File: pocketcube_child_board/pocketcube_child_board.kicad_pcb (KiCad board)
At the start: 2 copper layers, 50 x 50 mm, 3 parts, among them J1 M55-7101242R

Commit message: Fixed footprints
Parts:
- moved MOD1 0.54 mm to (106.0, 68.5)
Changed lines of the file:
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@@
 	(footprint "inspirefly:RFM98W-433S2"
 		(layer "F.Cu")
-		(at 106.2 68)
+		(at 106 68.5)
 		(property "Reference" "MOD1"
 			(at -4.825 -9.075 0)
@@
 		)
 		(embedded_fonts no)
-		(model "/Users/alexdiarra/Desktop/RFM98W-433S2.STEP 14.24.08"
+		(model "${KIPRJMOD}/3D Files/RFM98W-433S2.STEP"
 			(offset
 				(xyz 0 0 0)
@@
 		)
 		(embedded_fonts no)
-		(model "/Users/alexdiarra/Downloads/RF_Copper_Antenna_Model.STEP"
+		(model "${KIPRJMOD}/3D Files/RF_Copper_Antenna_Model.STEP"
 			(offset
 				(xyz 0 84.5 2)
@@
 		)
 		(embedded_fonts no)
-		(model "/Users/alexdiarra/Desktop/m55-7101242r.stp"
+		(model "${KIPRJMOD}/3D Files/m55-7101242r.stp"
 			(offset
 				(xyz 0 2.59 2)
@@
 		)
 	)
+	(gr_line
+		(start 115.5 75.5)
+		(end 126.5 75.5)
+		(stroke
+			(width 0.2)
+			(type default)
+		)
+		(layer "F.Cu")
+	)
+	(gr_line
+		(start 127.5 74.5)
+		(end 127.5 60.5)
+		(stroke
+			(width 0.2)
+			(type default)
+		)
+		(layer "F.Cu")
+	)
+	(gr_line
+		(start 126.5 75.5)
+		(end 127.5 74.5)
+		(stroke
+			(width 0.2)
+			(type default)
+		)
+		(layer "F.Cu")
+	)
 	(gr_rect

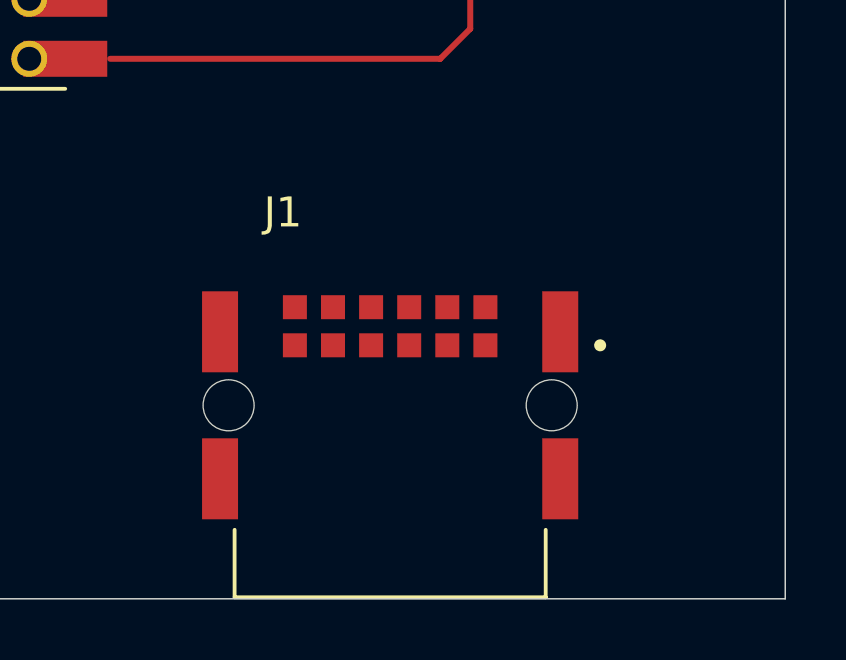
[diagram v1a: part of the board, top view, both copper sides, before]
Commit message: Added new connector to PCB
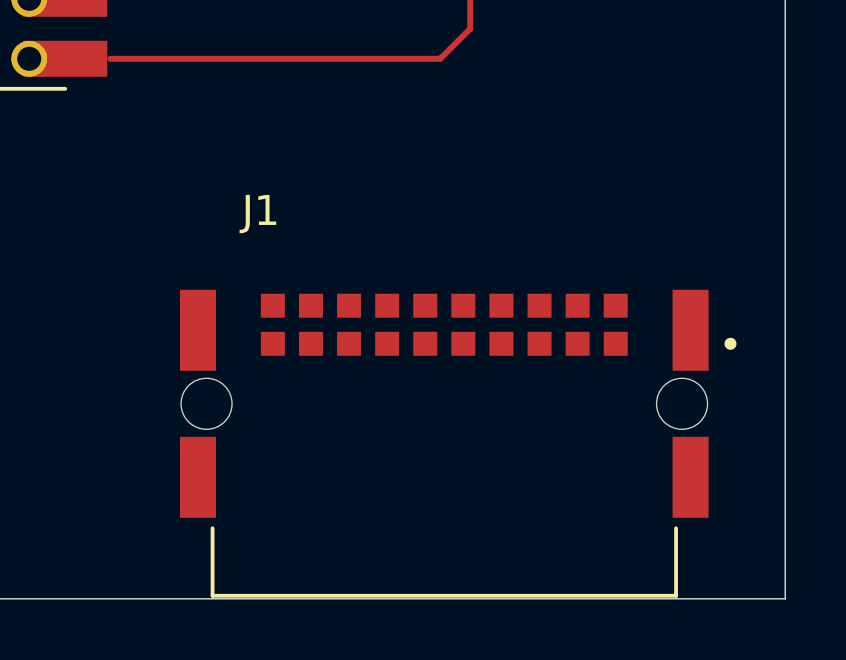
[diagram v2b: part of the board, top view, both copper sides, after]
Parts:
- J1: value M55-7101242R -> M55-7102042R; footprint inspirefly:HARWIN_M55-7101242R -> inspirefly:HARWIN_M55-7102042R
- moved J1 1.81 mm to (126.6, 87.0)
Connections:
- J1 pad A1: 3.3V -> unconnected-(J1-PadA1)
- J1 pad A2: CLK -> unconnected-(J1-PadA2)
- J1 pad A3: CS -> unconnected-(J1-PadA3)
- J1 pad A4: MISO -> 4.2V
- J1 pad A5: MOSI -> 3.3V
- J1 pad A6: GND -> CLK
- J1 pad B1: 3.3V -> unconnected-(J1-PadB1)
- J1 pad B2: CLK -> unconnected-(J1-PadB2)
- J1 pad B3: CS -> unconnected-(J1-PadB3)
- J1 pad B4: MISO -> 4.2V
- J1 pad B5: MOSI -> 3.3V
- J1 pad B6: GND -> CLK

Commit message: 11/2 via stitching v0.1
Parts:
- moved J1 27.9 mm to (104.5, 70.0)
- moved MOD1 16.1 mm to (104.0, 52.5)
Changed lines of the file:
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@@
 			(psa4output no)
 			(plot_black_and_white yes)
-			(plotinvisibletext no)
 			(sketchpadsonfab no)
 			(plotpadnumbers no)
@@
 	(footprint "inspirefly:RFM98W-433S2"
 		(layer "F.Cu")
-		(at 106 68.5)
+		(at 104 52.5)
 		(property "Reference" "MOD1"
 			(at -4.825 -9.075 0)
@@
 	(footprint "inspirefly:HARWIN_M55-7102042R"
 		(layer "F.Cu")
-		(at 126.635 87)
+		(at 104.5 70)
 		(property "Reference" "J1"
 			(at -6.115 -6.425 0)

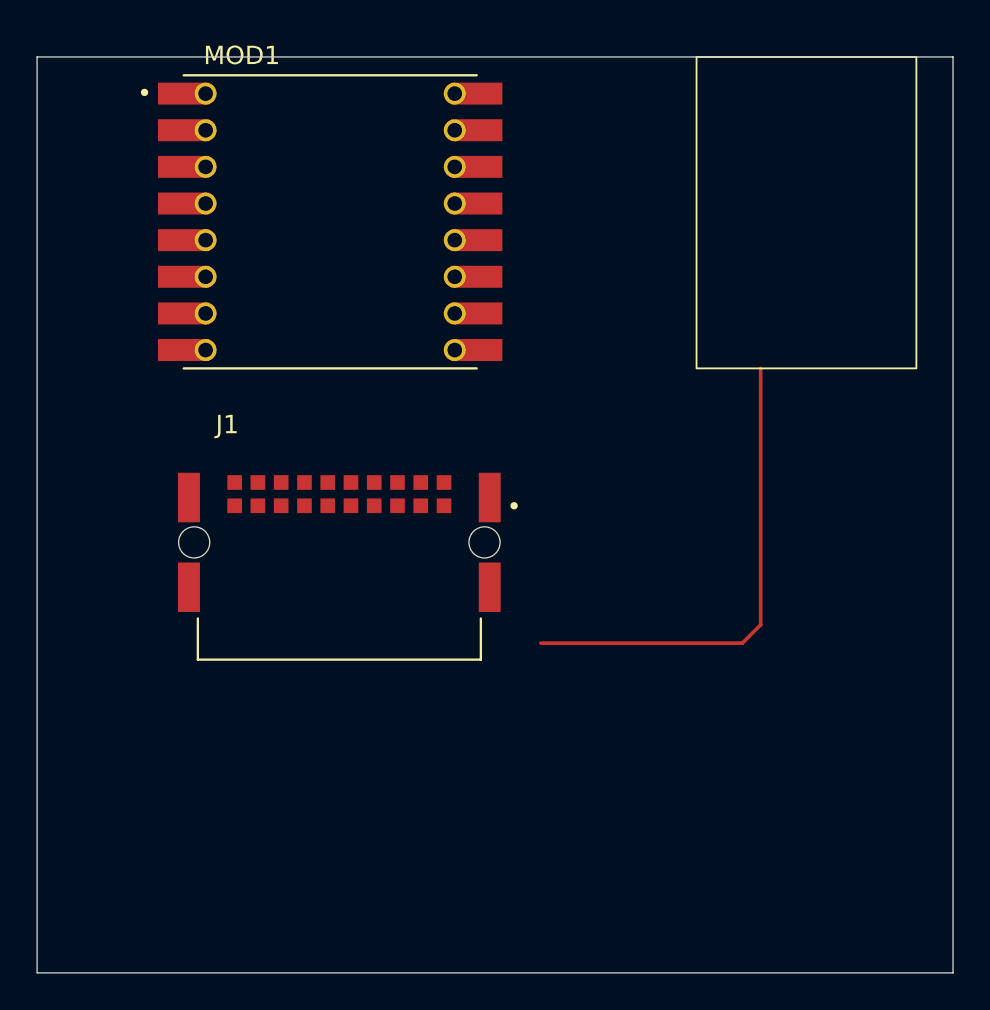
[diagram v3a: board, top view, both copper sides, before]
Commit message: Edited PCB Layout & Rearranged Pins
I restructured the layout of the PCB due to traces going under the components, I also changed the pin order of the connector to add with routing
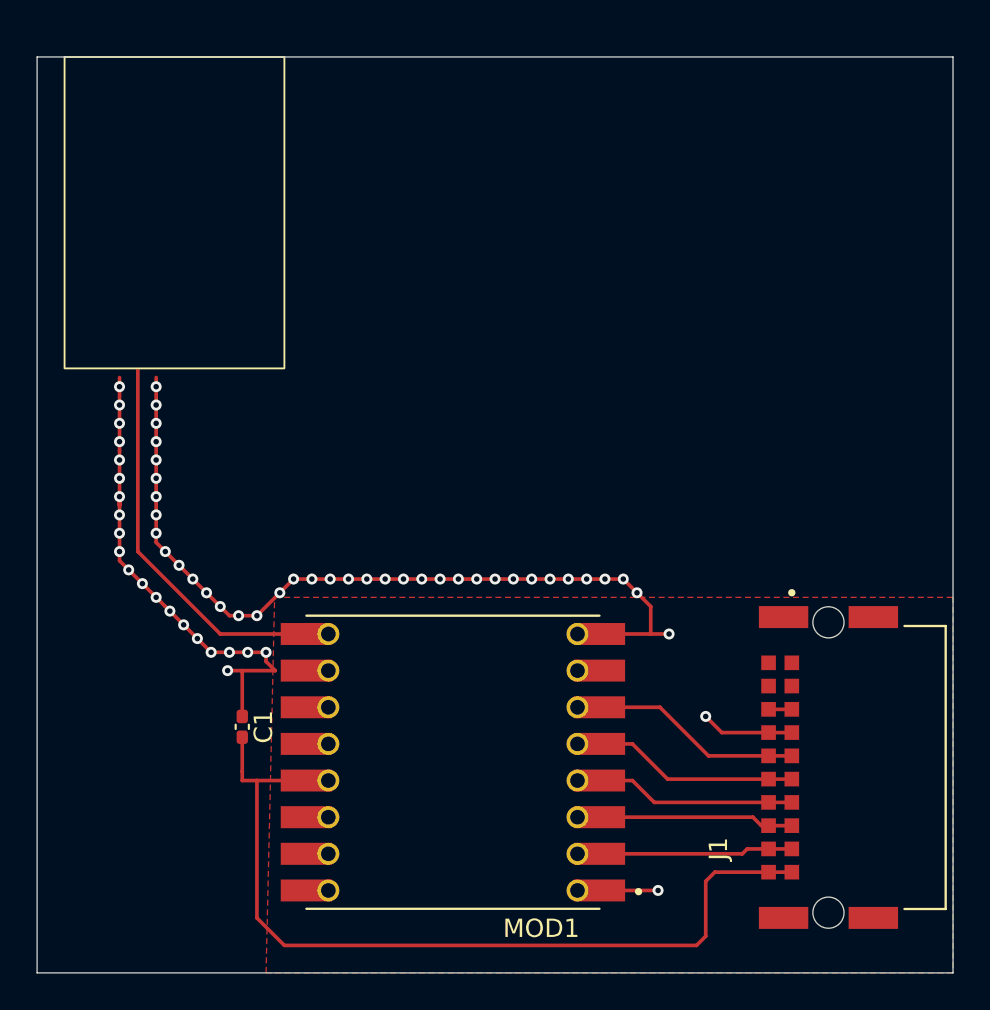
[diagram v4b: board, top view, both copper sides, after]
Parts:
- added C1: 100nF, Capacitor_SMD:C_0402_1005Metric_Pad0.74x0.62mm_HandSolder, F.Cu at (99.2, 80.1)
- moved AE1 34.5 mm to (95.5, 52.5)
- moved MOD1 30.3 mm to (110.7, 82.0), turned to 180 degrees
- moved J1 29.4 mm to (131.2, 82.3), turned to 90 degrees
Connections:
- J1 pad A10: GND -> 3.3V
- J1 pad A3: unconnected-(J1-PadA3) -> 4.2V
- J1 pad A4: 4.2V -> GND
- J1 pad A5: 3.3V -> RFM_RESET
- J1 pad A6: CLK -> CS
- J1 pad A7: CS -> CLK
- J1 pad A8: MISO -> MOSI
- J1 pad A9: MOSI -> MISO
- J1 pad B10: GND -> 3.3V
- J1 pad B3: unconnected-(J1-PadB3) -> 4.2V
- J1 pad B4: 4.2V -> GND
- J1 pad B5: 3.3V -> RFM_RESET
- J1 pad B6: CLK -> CS
- J1 pad B7: CS -> CLK
- J1 pad B8: MISO -> MOSI
- J1 pad B9: MOSI -> MISO
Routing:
- net GND: track 0.00 -> 80.1 mm, vias 0 -> 61
- net 3.3V: track 0.00 -> 46.6 mm
- net Net-(AE1-A): track 0.00 -> 21.0 mm
- net MOSI: track 0.00 -> 11.6 mm
- net RFM_RESET: track 0.00 -> 11.6 mm
- net MISO: track 0.00 -> 11.5 mm
- net CS: track 0.00 -> 11.3 mm
- net CLK: track 0.00 -> 11.0 mm
- net 4.2V: track 0.00 -> 1.27 mm
- added copper zone on F.Cu, net 3.3V

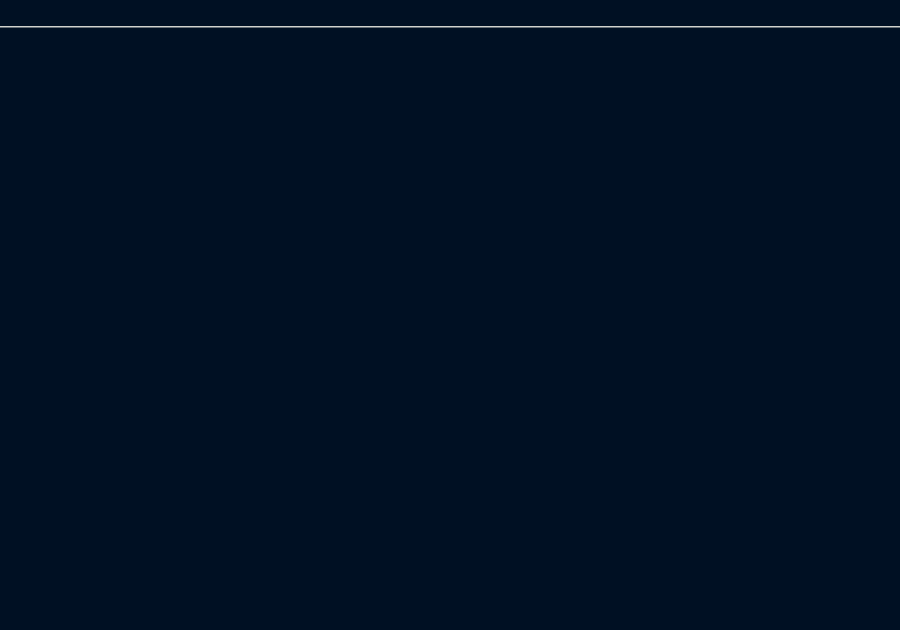
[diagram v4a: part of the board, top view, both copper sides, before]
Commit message: Added SI3477DV-T1-GE3 P-Channel MOSFET to Schematic and PCB
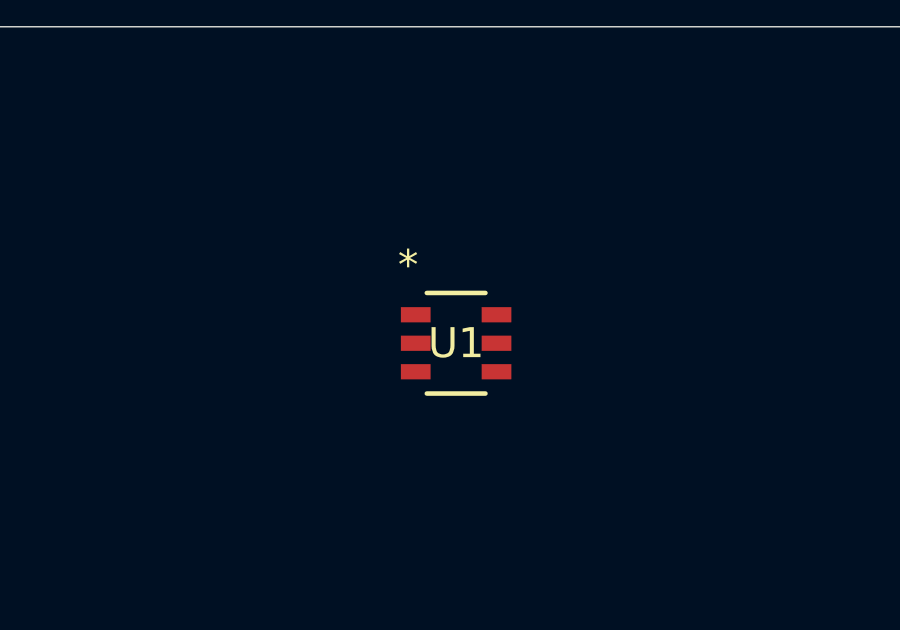
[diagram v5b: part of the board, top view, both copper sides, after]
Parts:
- added U1: SI3477DV-T1-GE3, inspirefly:SOT_V-T1-GE3_VIS, F.Cu at (122.2, 54.1)

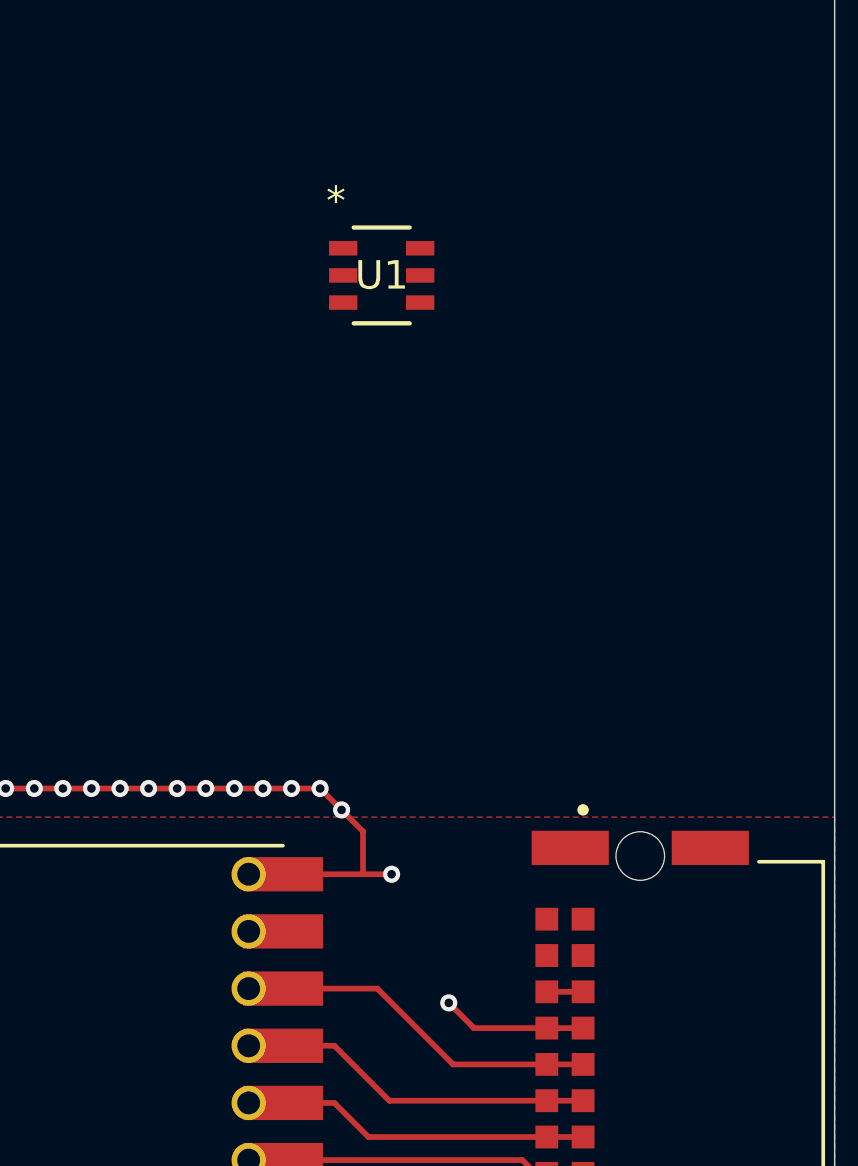
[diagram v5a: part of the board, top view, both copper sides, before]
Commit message: Integrating P-Channel MOSFET
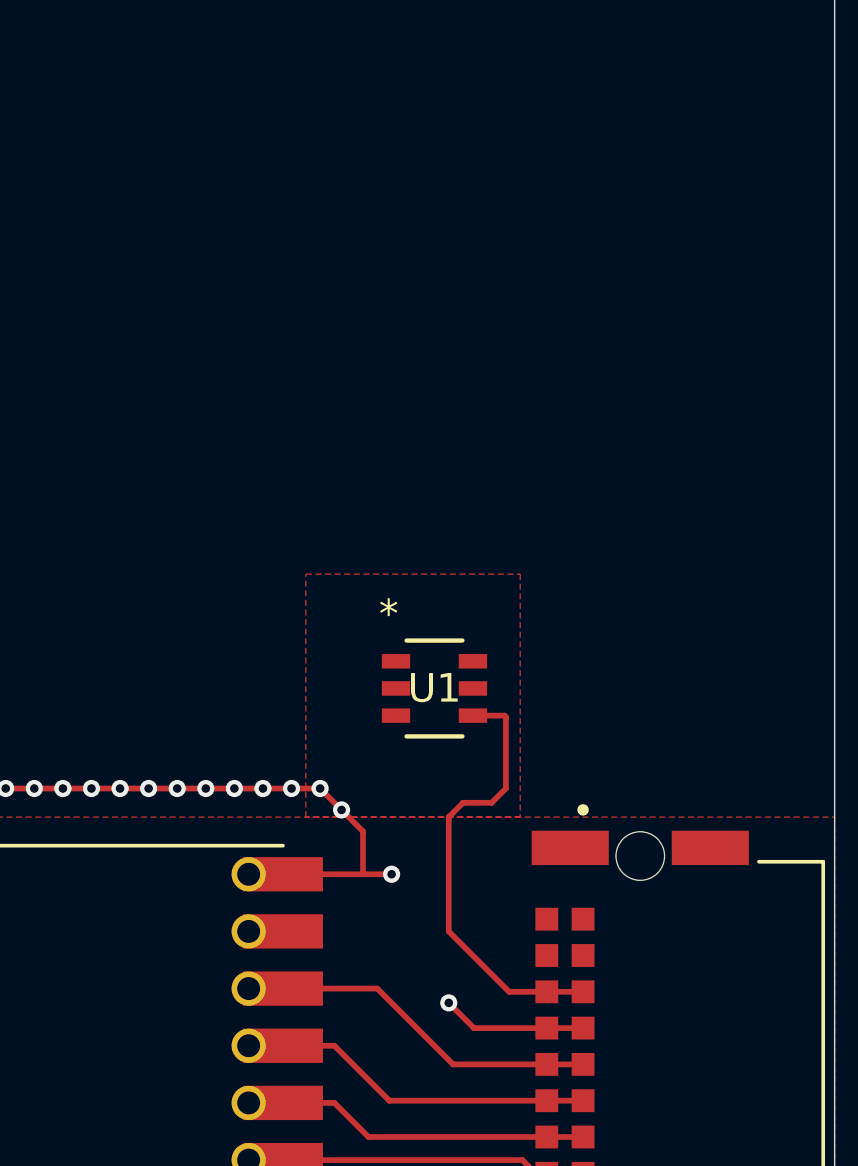
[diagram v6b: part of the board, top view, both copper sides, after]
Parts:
- moved U1 14.6 mm to (124.0, 68.5)
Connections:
- U1 pad 4: unconnected-(U1-S-Pad4) -> 4.2V
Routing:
- net 4.2V: track 1.27 -> 15.7 mm
- added copper zone on F.Cu, net 4.2V
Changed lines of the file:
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@@
 	(net 29 "unconnected-(U1-D-Pad6)")
 	(net 30 "unconnected-(U1-D-Pad2)")
-	(net 31 "unconnected-(U1-S-Pad4)")
 	(footprint "inspirefly:RFM98W-433S2"
 		(layer "F.Cu")
@@
 	(footprint "inspirefly:SOT_V-T1-GE3_VIS"
 		(layer "F.Cu")
-		(at 122.1538 54.05004)
+		(at 124 68.5)
 		(tags "SI3477DV-T1-GE3 ")
 		(property "Reference" "U1"
@@
 			(size 0.9906 0.508)
 			(layers "F.Cu" "F.Mask" "F.Paste")
-			(net 31 "unconnected-(U1-S-Pad4)")
+			(net 21 "4.2V")
 			(pinfunction "S")
 			(pintype "unspecified")
@@
 	)
 	(segment
+		(start 125 72.5)
+		(end 126 72.5)
+		(width 0.2)
+		(layer "F.Cu")
+		(net 21)
+	)
+	(segment
+		(start 126.6125 79.1125)
+		(end 124.5 77)
+		(width 0.2)
+		(layer "F.Cu")
+		(net 21)
+	)
+	(segment
+		(start 127.93 79.1125)
+		(end 126.6125 79.1125)
+		(width 0.2)
+		(layer "F.Cu")
+		(net 21)
+	)
+	(segment
+		(start 126.5 72)
+		(end 126.5 69.5)
+		(width 0.2)
+		(layer "F.Cu")
+		(net 21)
+	)
+	(segment
+		(start 126.5 69.5)
+		(end 126.44996 69.44996)
+		(width 0.2)
+		(layer "F.Cu")
+		(net 21)
+	)
+	(segment
+		(start 124.5 77)
+		(end 124.5 73)
+		(width 0.2)
+		(layer "F.Cu")
+		(net 21)
+	)
+	(segment
+		(start 124.5 73)
+		(end 125 72.5)
+		(width 0.2)
+		(layer "F.Cu")
+		(net 21)
+	)
+	(segment
+		(start 126.44996 69.44996)
+		(end 125.3462 69.44996)
+		(width 0.2)
+		(layer "F.Cu")
+		(net 21)
+	)
+	(segment
 		(start 127.93 79.1125)
 		(end 129.2 79.1125)
@@
 		(net 21)
 	)
+	(segment
+		(start 127.93 79.1125)
+		(end 128 79.1125)
+		(width 0.2)
+		(layer "F.Cu")
+		(net 21)
+	)
+	(segment
+		(start 126 72.5)
+		(end 126.5 72)
+		(width 0.2)
+		(layer "F.Cu")
+		(net 21)
+	)
+	(zone
+		(net 21)
+		(net_name "4.2V")
+		(layer "F.Cu")
+		(hatch edge 0.5)
+		(priority 1)
+		(connect_pads
+			(clearance 0)
+		)
+		(min_thickness 0.25)
+		(filled_areas_thickness no)
+		(fill yes
+			(thermal_gap 0.5)
+			(thermal_bridge_width 0.5)
+		)
+		(polygon
+			(pts
+				(xy 119.5 64.5) (xy 127 64.5) (xy 127 73) (xy 119.5 73)
+			)
+		)
+	)
 	(zone
